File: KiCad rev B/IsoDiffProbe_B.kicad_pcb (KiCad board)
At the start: 2 copper layers, 77.2 x 49.1 mm, 82 parts, among them J1 USB C 6-Pin, J2 SMA Conn, P1 Header 10X2, U1 AMC3, U2 TLC272ID

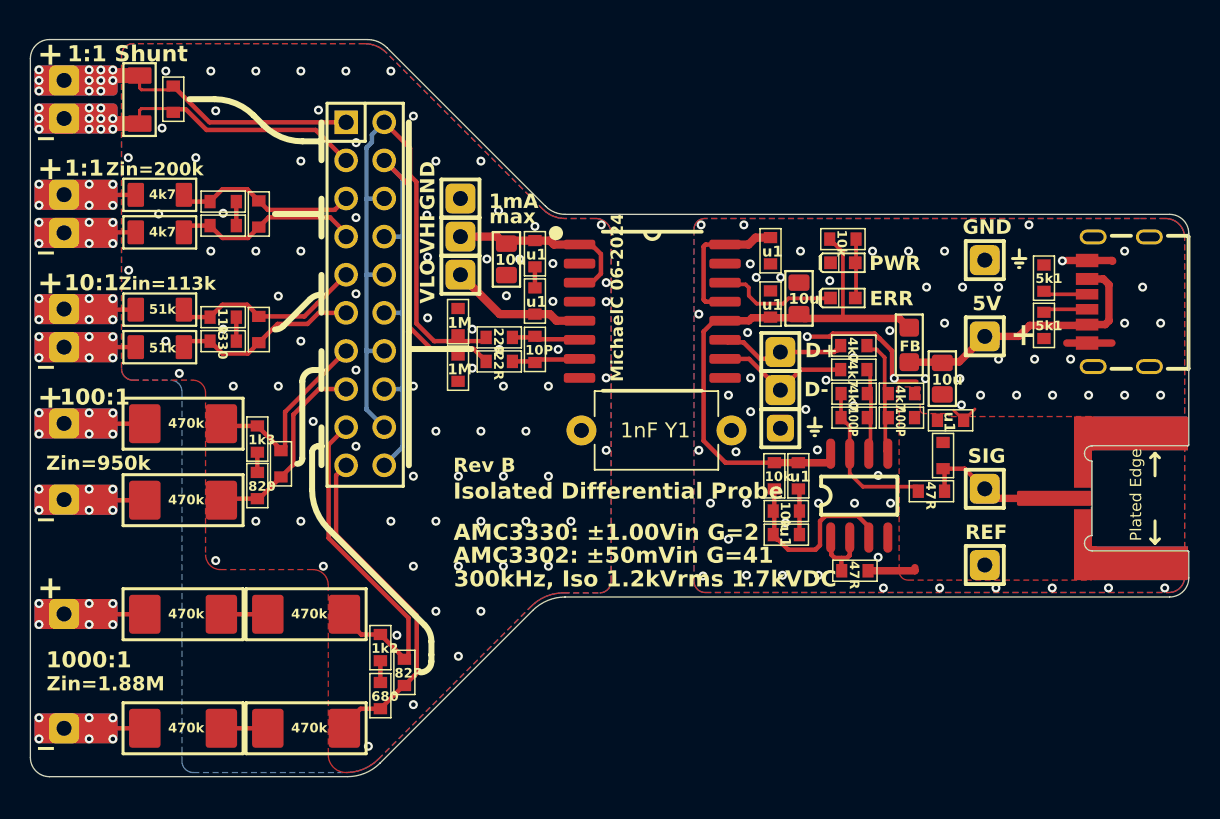
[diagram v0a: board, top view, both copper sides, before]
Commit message: Value changes to improve rev A1->A2 and updated rev B design.
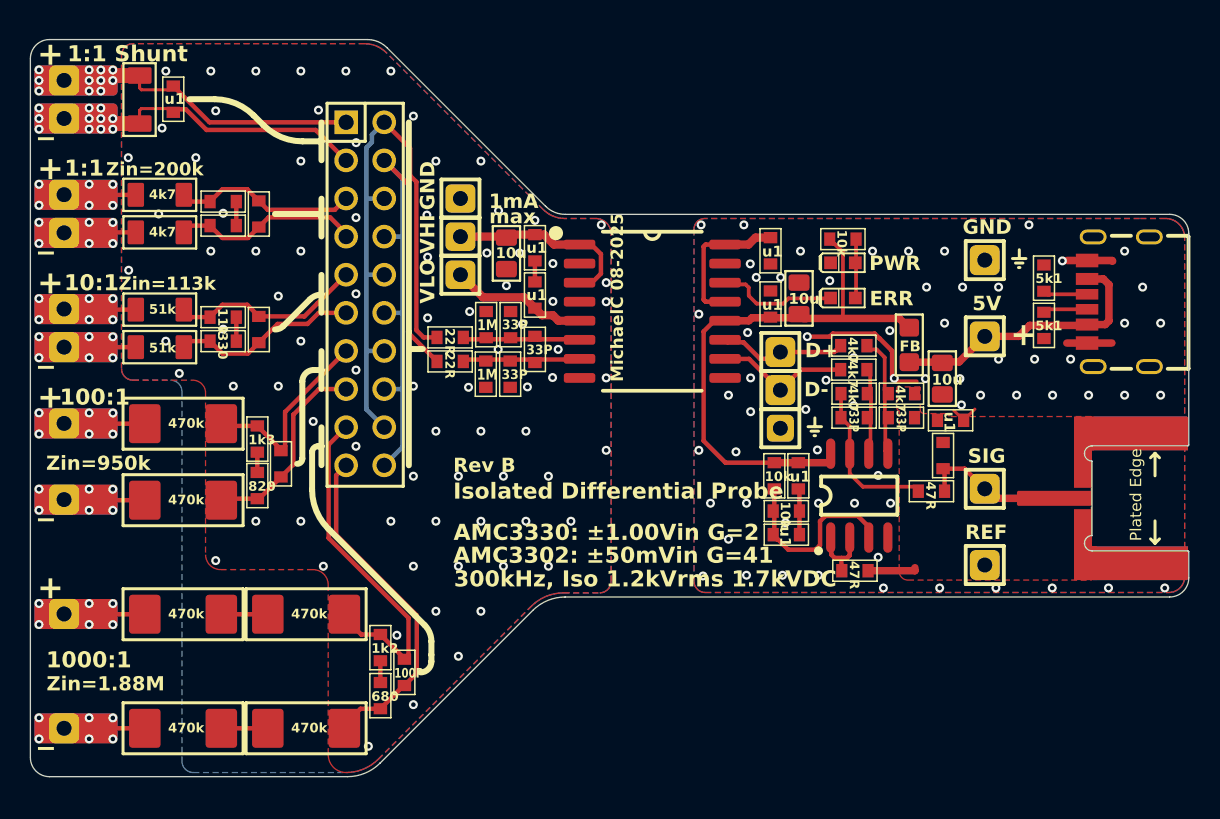
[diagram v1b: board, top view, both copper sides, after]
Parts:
- removed Cmod1: 1nF Y1, Capacitor_THT:C_Disc_D8.0mm_W5.0mm_P10.00mm
- added C20: 10pF, NixieClock_RevA.PcbLib:0603, F.Cu at (141.9, 98.6)
- added C21: 10pF, NixieClock_RevA.PcbLib:0603, F.Cu at (141.9, 101.9)
- moved R11 3.28 mm to (138.8, 100.3)
- moved R13 3.28 mm to (138.8, 101.9)
- moved R33 1.89 mm to (140.3, 101.9)
- moved R34 1.89 mm to (140.3, 98.6)
- moved C10 0.40 mm to (143.5, 98.3)
- moved C4 0.40 mm to (141.6, 95.8)
- moved C5 0.40 mm to (143.5, 93.4)
- renumbered Rmod2 to R33, Rmod1 to R34
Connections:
- R33 pad 1: NetP1_4 -> NetC11_2
- R34 pad 2: NetP1_2 -> NetC11_1
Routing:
- net NetC11_1: track 4.59 -> 8.08 mm
- net NetC11_2: track 4.61 -> 7.99 mm
- net NetP1_2: track 44.4 -> 41.2 mm
- net NetP1_4: track 42.9 -> 39.9 mm
- net ISOPWR: track 13.0 -> 12.1 mm
- net HGND: vias 82 -> 83
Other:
- board text added: "33P"
- board text added: "MichaelC 08-2025"
- board text removed: "10P"
- board text removed: "82P"
- board text removed: "MichaelC 06-2024"
